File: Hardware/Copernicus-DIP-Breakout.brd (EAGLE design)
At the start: 31.8 x 27.9 mm, 13 parts, among them U1 COPERNICUS

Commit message: Fix silk screen on board file
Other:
- board text added: "VBAT"
- board text removed: "BOOT"
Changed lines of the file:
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@@
 <circle x="-1.27" y="0" radius="0.016" width="0" layer="47"/>
 <text x="26.475" y="23.746" size="1.778" layer="22" ratio="15" rot="MR270">LNA</text>
-<text x="23.935" y="23.746" size="1.778" layer="22" ratio="15" rot="MR270">R1</text>
+<text x="23.935" y="23.746" size="1.778" layer="22" ratio="15" rot="MR270">VBAT</text>
 <text x="21.395" y="23.746" size="1.778" layer="22" ratio="15" rot="MR270">OPEN</text>
 <text x="18.855" y="23.746" size="1.778" layer="22" ratio="15" rot="MR270">SHORT</text>
-<text x="16.315" y="23.746" size="1.778" layer="22" ratio="15" rot="MR270">R2</text>
-<text x="13.775" y="23.746" size="1.778" layer="22" ratio="15" rot="MR270">BOOT</text>
+<text x="16.315" y="23.746" size="1.778" layer="22" ratio="15" rot="MR270">R1</text>
+<text x="13.775" y="23.746" size="1.778" layer="22" ratio="15" rot="MR270">R2</text>
 <text x="11.235" y="23.746" size="1.778" layer="22" ratio="15" rot="MR270">XRST</text>
 <text x="8.695" y="23.746" size="1.778" layer="22" ratio="15" rot="MR270">VCC</text>
@@
 <contactref element="JP3" pad="GND@1"/>
 <contactref element="U1" pad="15"/>
-<contactref element="JP1" pad="9"/>
 <contactref element="U1" pad="13"/>
 <via x="20.32" y="10.16" extent="1-16" drill="0.508"/>
@@
 <contactref element="U1" pad="28"/>
 <contactref element="U1" pad="27"/>
+<contactref element="JP1" pad="9"/>
+<wire x1="29.21" y1="20.32" x2="29.21" y2="22.86" width="0" layer="19" extent="1-1"/>
+<wire x1="27.32" y1="19.05" x2="29.21" y2="20.32" width="0" layer="19" extent="1-1"/>
+<wire x1="27.32" y1="15.24" x2="27.32" y2="19.05" width="0" layer="19" extent="1-1"/>
+<wire x1="27.94" y1="12.7" x2="27.32" y2="15.24" width="0" layer="19" extent="1-1"/>
+<wire x1="29.21" y1="12.7" x2="27.94" y2="12.7" width="0" layer="19" extent="1-1"/>
+<wire x1="29.464" y1="10.795" x2="29.21" y2="12.7" width="0" layer="19" extent="1-1"/>
+<wire x1="29.464" y1="10.795" x2="29.464" y2="10.795" width="0" layer="19" extent="1-16"/>
+<wire x1="23.0632" y1="20.955" x2="27.32" y2="19.05" width="0" layer="19" extent="1-1"/>
+<wire x1="23.0632" y1="22.225" x2="23.0632" y2="20.955" width="0" layer="19" extent="1-1"/>
+<wire x1="29.464" y1="5.715" x2="29.464" y2="10.795" width="0" layer="19" extent="1-16"/>
+<wire x1="29.464" y1="5.715" x2="29.464" y2="5.715" width="0" layer="19" extent="1-16"/>
+<wire x1="29.21" y1="3.81" x2="29.464" y2="5.715" width="0" layer="19" extent="16-16"/>
+<wire x1="27.94" y1="3.81" x2="29.21" y2="3.81" width="0" layer="19" extent="1-1"/>
+<wire x1="23.0632" y1="5.715" x2="27.94" y2="3.81" width="0" layer="19" extent="1-1"/>
+<wire x1="23.0632" y1="6.985" x2="23.0632" y2="5.715" width="0" layer="19" extent="1-1"/>
+<wire x1="23.0632" y1="9.525" x2="23.0632" y2="6.985" width="0" layer="19" extent="1-1"/>
+<wire x1="20.32" y1="7.112" x2="23.0632" y2="6.985" width="0" layer="19" extent="1-1"/>
+<wire x1="20.32" y1="10.16" x2="23.0632" y2="9.525" width="0" layer="19" extent="1-1"/>
+<wire x1="4.699" y1="6.985" x2="20.32" y2="7.112" width="0" layer="19" extent="1-1"/>
+<wire x1="4.699" y1="5.715" x2="4.699" y2="6.985" width="0" layer="19" extent="1-1"/>
+<wire x1="1.27" y1="7.62" x2="4.699" y2="6.985" width="0" layer="19" extent="1-1"/>
+<wire x1="1.27" y1="5.08" x2="1.27" y2="7.62" width="0" layer="19" extent="1-1"/>
+<wire x1="4.699" y1="22.225" x2="1.27" y2="7.62" width="0" layer="19" extent="1-1"/>
+<wire x1="5.08" y1="25.4" x2="4.699" y2="22.225" width="0" layer="19" extent="1-1"/>
 </signal>
 <signal name="VCC">

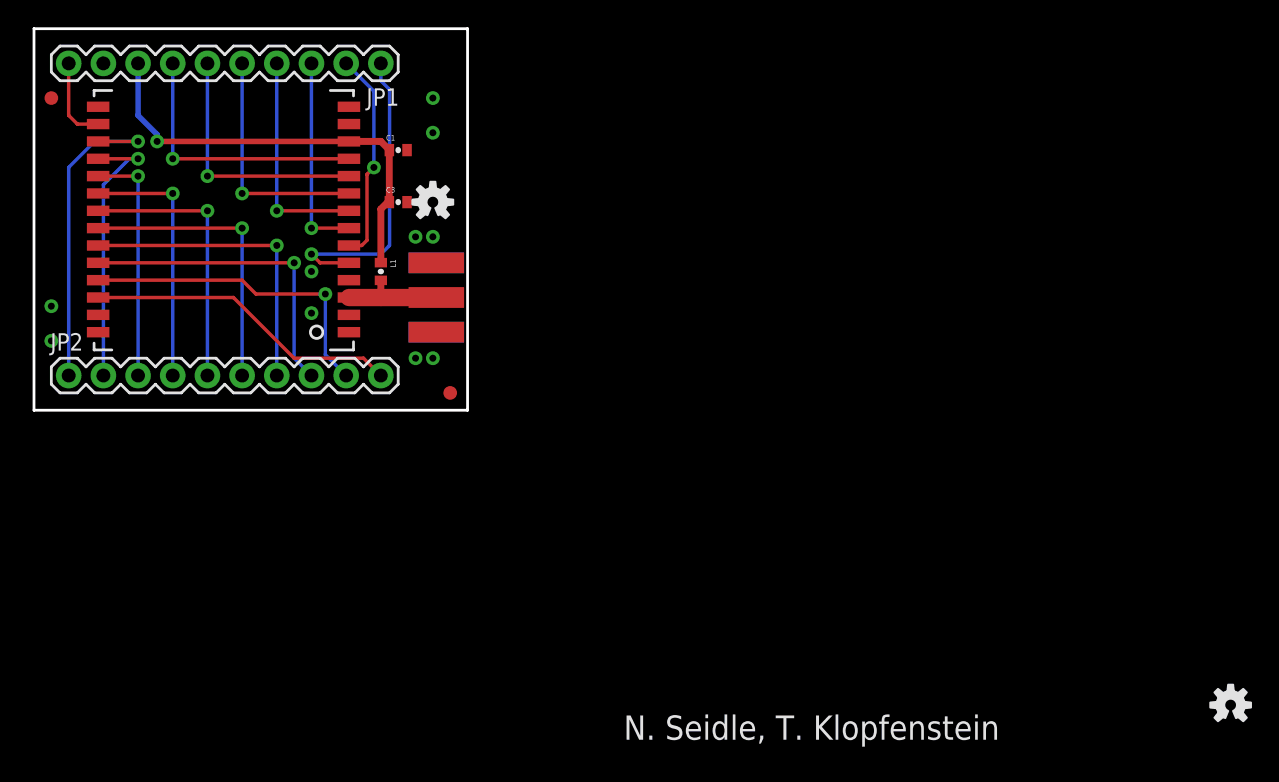
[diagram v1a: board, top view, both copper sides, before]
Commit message: Updated board to proper pin names, added in connection between XSTBY and Vcc, changed caps and inductor to 0603 package, and decreased PCB size.
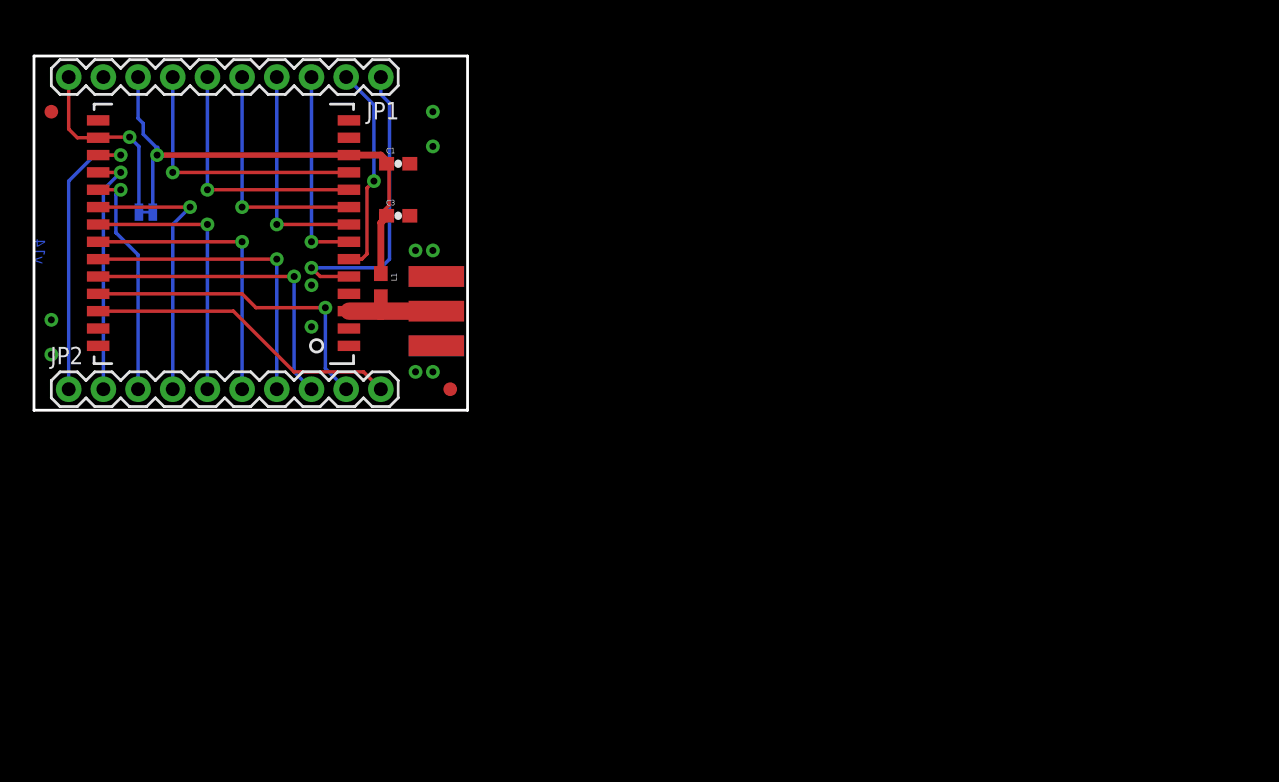
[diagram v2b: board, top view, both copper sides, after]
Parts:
- removed LOGO1: OSHW-LOGOS, SparkFun-Aesthetics:OSHW-LOGO-S
- removed U$5: (no value), SparkFun-Aesthetics:OSHW-LOGO-S
- added JP4: LOGO-SFESK, SparkFun-Aesthetics:SFE-LOGO-FLAME
- added SJ1: SOLDERJUMPERTRACE, SparkFun-Passives:SJ_2S-TRACE
- C1, C3: device SparkFun:0402-CAP -> SparkFun-Passives:0603-CAP
- L1: device SparkFun:0402-CAP -> SparkFun-Passives:0603
- U$1: value LOGO-SFENEW -> OSHW-LOGOS; device SparkFun:SFE-NEW-WEBLOGO -> SparkFun-Aesthetics:OSHW-LOGO-S
- moved U$1 20.6 mm to (3.54, 8.16)
- moved C1 1.00 mm to (26.7, 18.1)
- moved C3 1.00 mm to (26.7, 14.2)
- moved FRAME1 1.00 mm to (11.2, -22.9)
- moved JP1 1.00 mm to (25.4, 24.4)
- moved JP2 1.00 mm to (2.54, 1.54)
- moved JP3 1.00 mm to (29.5, 9.79)
- moved L1 1.00 mm to (25.4, 9.16)
- moved U$2 1.00 mm to (1.27, 21.9)
- moved U1 1.00 mm to (4.70, 4.71)
- moved U$3 0.27 mm to (30.5, 1.54)
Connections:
- net VCC: now also SJ1.1
- net XSTBY: now also SJ1.2
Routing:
- net XSTBY: track 6.23 -> 14.3 mm, vias 0 -> 1
- net VCC: track 32.2 -> 37.8 mm
- net R3: track 24.0 -> 21.5 mm
- net R4: track 20.2 -> 18.1 mm
- net RX-B: track 18.8 -> 20.6 mm
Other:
- board size 31.8 x 27.9 mm -> 31.8 x 25.9 mm
- board text added: "Copernicus II DIP"
- board text added: "N. Seidle, Updated by: T. Klopfenstein"
- board text added: "v14"
- board text removed: "1100.00"
- board text removed: "N. Seidle, T. Klopfenstein"
